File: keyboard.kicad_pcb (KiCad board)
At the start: 2 copper layers, 285 x 94.6 mm, 190 parts, among them IC1 ATMEGA32U4, J1 MINI, P1 CONN_1, P10 CONN_1, P16 CONN_1, P17 CONN_1, P2 CONN_1, P3 CONN_1, P37 CONN_1, P38 CONN_1, P39 CONN_1, P4 CONN_1, P40 CONN_1, P41 CONN_1, P42 CONN_1, P5 CONN_1, P6 CONN_1, P7 CONN_1, P8 CONN_1, P9 CONN_1, X1 ASX3F

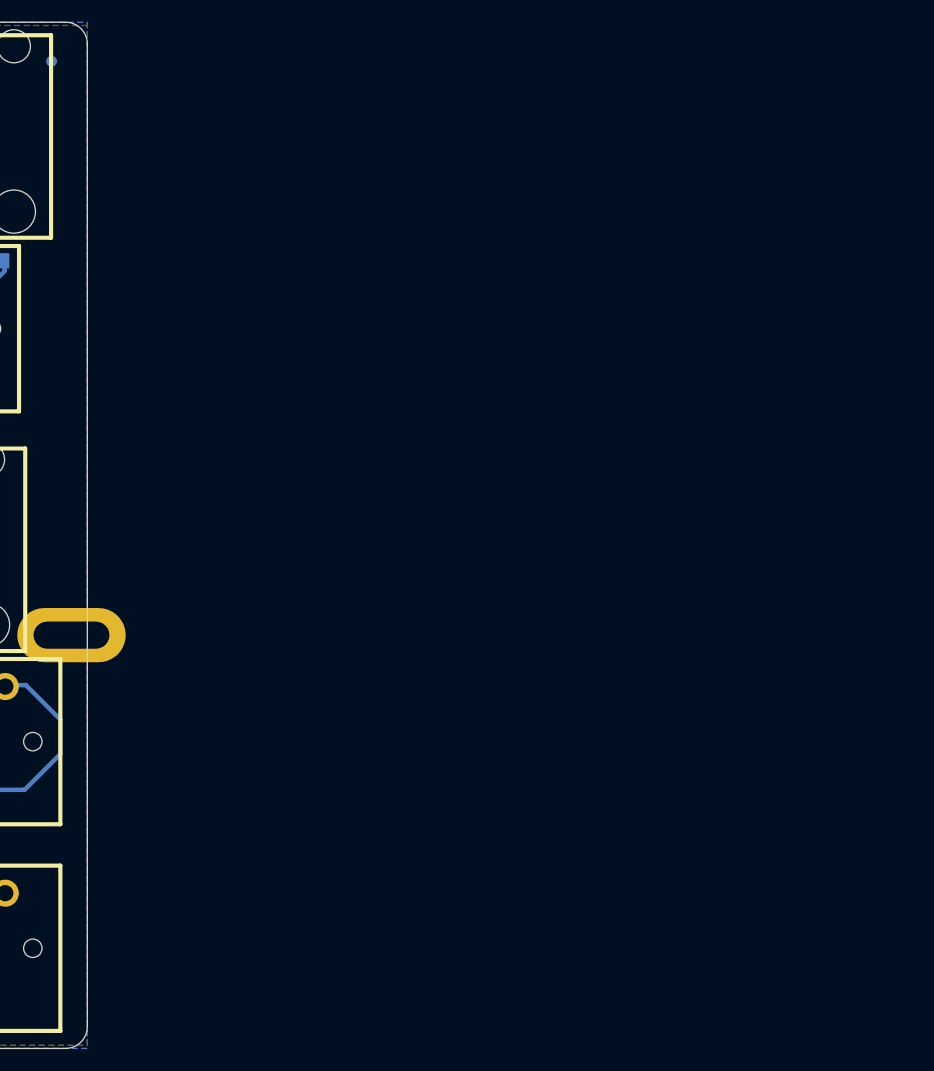
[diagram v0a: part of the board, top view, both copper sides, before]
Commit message: Extend edge cuts to accommodate numpad
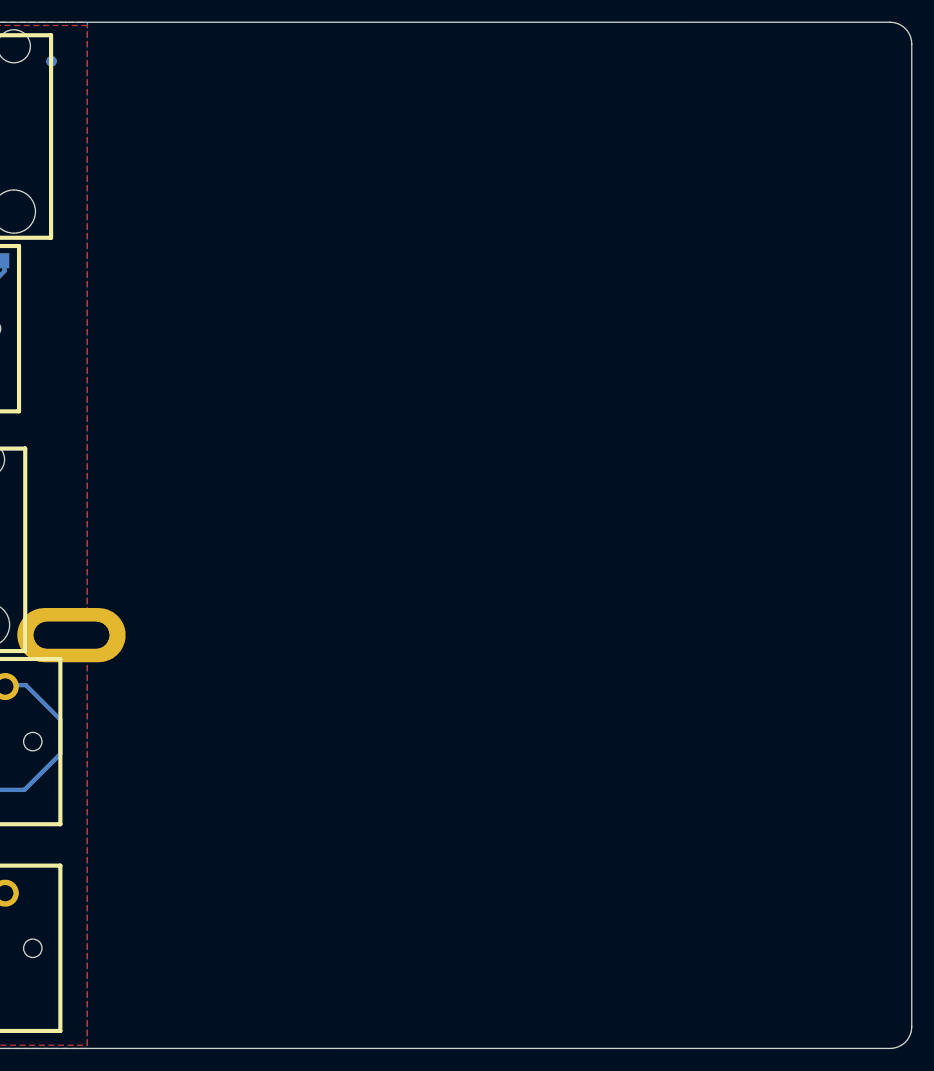
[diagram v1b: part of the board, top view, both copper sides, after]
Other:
- board size 285 x 94.6 mm -> 361 x 94.6 mm
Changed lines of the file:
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@@
   (general
     (thickness 1.6002)
-    (drawings 323)
+    (drawings 325)
     (tracks 2026)
     (zones 0)
@@
   )
   (layers
-    (0 F.Cu signal)
+    (0 F.Cu signal hide)
     (31 B.Cu signal hide)
     (32 B.Adhes user hide)
@@
     (40 Dwgs.User user)
     (41 Cmts.User user hide)
-    (42 Eco1.User user)
+    (42 Eco1.User user hide)
     (43 Eco2.User user hide)
-    (44 Edge.Cuts user hide)
+    (44 Edge.Cuts user)
     (48 B.Fab user hide)
     (49 F.Fab user hide)
@@
     )
   )
+  (gr_line (start 345.29 64.62) (end 421.29 64.6212) (layer Edge.Cuts) (width 0.0991))
+  (gr_line (start 345.29 159.22) (end 421.29 159.2212) (layer Edge.Cuts) (width 0.0991))
+  (gr_arc (start 421.29 66.6212) (end 421.29 64.6212) (angle 90) (layer Edge.Cuts) (width 0.0991))
+  (gr_arc (start 421.29 157.2212) (end 423.29 157.2212) (angle 90) (layer Edge.Cuts) (width 0.0991))
+  (gr_line (start 423.29 66.62) (end 423.29 157.2224) (angle 90) (layer Edge.Cuts) (width 0.0991))
   (gr_line (start 346.75064 140.12672) (end 403.75064 140.13434) (layer Dwgs.User) (width 0.381))
   (gr_line (start 346.75064 83.12658) (end 422.75064 83.1342) (layer Dwgs.User) (width 0.381))
@@
   (gr_arc (start 64.29 66.62) (end 62.29 66.62) (angle 90) (layer Edge.Cuts) (width 0.0991))
   (gr_arc (start 64.29 157.22) (end 64.29 159.22) (angle 90) (layer Edge.Cuts) (width 0.0991))
-  (gr_arc (start 345.29 157.22) (end 347.29 157.22) (angle 90) (layer Edge.Cuts) (width 0.0991))
-  (gr_arc (start 345.29 66.62) (end 345.29 64.62) (angle 90) (layer Edge.Cuts) (width 0.0991))
   (gr_line (start 62.29 157.2212) (end 62.29 66.6188) (angle 90) (layer Edge.Cuts) (width 0.0991))
   (gr_line (start 345.29 159.22) (end 64.29 159.22) (angle 90) (layer Edge.Cuts) (width 0.0991))
-  (gr_line (start 347.29 66.6188) (end 347.29 157.2212) (angle 90) (layer Edge.Cuts) (width 0.0991))
   (gr_line (start 64.29 64.62) (end 345.29 64.62) (angle 90) (layer Edge.Cuts) (width 0.0991))
   (gr_line (start 330.12888 214.94242) (end 330.12888 130.62966) (angle 90) (layer Eco2.User) (width 0.381))

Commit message: Remove GPIOs
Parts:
- removed P10, P38, P39, P40, P41, P7, P8, P9: CONN_1, pad
- removed R10, R11, R12, R6, R7, R8, R9: R, res:resistor
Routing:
- net /GPIO1: track 398.3 -> 0.00 mm, vias 4 -> 0
- net /GPIO3: track 385.2 -> 0.00 mm, vias 7 -> 0
- net /GPIO2: track 372.2 -> 0.00 mm, vias 6 -> 0
- net /GPIO0: track 291.9 -> 0.00 mm, vias 5 -> 0
- net /row5: track 327.2 -> 313.9 mm

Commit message: Start remapping of rows and cols in MCU
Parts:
- removed MXWIRE (x4): VAL**, MX1A-wire
- removed P1, P16, P17, P2, P3, P37, P4, P42, P5, P6: CONN_1, pad
- moved R3 12.6 mm to (154.0, 155.6)
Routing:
- net GND: track 686.3 -> 75.8 mm, vias 41 -> 0
- net VCC: track 384.0 -> 217.1 mm, vias 6 -> 0
- net /col13: track 239.2 -> 85.7 mm, vias 2 -> 0
- net /col12: track 225.0 -> 91.9 mm, vias 2 -> 0
- net /row5: track 313.9 -> 201.1 mm, vias 2 -> 0
- net /col11: track 203.0 -> 90.5 mm, vias 2 -> 0
- net /col1: track 166.1 -> 68.7 mm, vias 2 -> 0
- net /col10: track 185.8 -> 92.1 mm, vias 2 -> 0
- net /MOSI: track 85.2 -> 0.00 mm, vias 1 -> 0
- net /col6: track 156.9 -> 94.8 mm
- net /col9: track 129.9 -> 67.9 mm, vias 2 -> 0
- net /col2: track 143.4 -> 81.5 mm, vias 4 -> 2
- net /col4: track 106.4 -> 56.4 mm, vias 2 -> 0
- net /MISO: track 324.3 -> 278.1 mm, vias 5 -> 4
- net /~RES~: track 179.2 -> 133.7 mm
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
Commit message: Connected all rows in PCB
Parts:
- removed FID (x2): FIDUCIAL, hole:FIDUCIAL
- moved C3 7.93 mm to (161.7, 139.8), turned to 90 degrees
- moved R3 4.24 mm to (150.7, 152.8), turned to 90 degrees
- moved C6 3.41 mm to (168.5, 155.7), turned to 0 degrees
- moved C4 0.68 mm to (152.7, 152.7), turned to 90 degrees
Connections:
- net /GPIO0 renamed Net-(IC1-Pad36)
- net /GPIO1 renamed Net-(IC1-Pad37)
- net /GPIO2 renamed Net-(IC1-Pad38)
- net /GPIO3 renamed Net-(IC1-Pad39)
- net /~RES~ renamed Net-(IC1-Pad13)
- D36 pad 1: /SCK -> /col8
- D37 pad 1: /SCK -> /col8
- D38 pad 1: /SCK -> /col8
- D39 pad 1: /SCK -> /col8
- D66 pad 1: /MISO -> /col14
- D67 pad 1: /MISO -> /col14
- D68 pad 1: /MISO -> /col14
- D69 pad 1: /MISO -> /col14
- D70 pad 1: /MISO -> /col14
- IC1 pad 1: /col3 -> Net-(IC1-Pad1)
- IC1 pad 10: /MOSI -> /row3
- IC1 pad 11: /MISO -> /row4
- IC1 pad 12: /col9 -> Net-(IC1-Pad12)
- IC1 pad 18: /row1 -> Net-(IC1-Pad18)
- IC1 pad 19: /row2 -> Net-(IC1-Pad19)
- IC1 pad 20: /row3 -> Net-(IC1-Pad20)
- IC1 pad 21: /row4 -> Net-(IC1-Pad21)
- IC1 pad 25: /col7 -> Net-(IC1-Pad25)
- IC1 pad 26: /col13 -> Net-(IC1-Pad26)
- IC1 pad 27: /col12 -> Net-(IC1-Pad27)
- IC1 pad 28: /col11 -> Net-(IC1-Pad28)
- IC1 pad 29: /col10 -> Net-(IC1-Pad29)
- IC1 pad 30: /col6 -> Net-(IC1-Pad30)
- IC1 pad 31: /col5 -> Net-(IC1-Pad31)
- IC1 pad 32: /col4 -> Net-(IC1-Pad32)
- IC1 pad 40: /col2 -> Net-(IC1-Pad40)
- IC1 pad 41: /col1 -> Net-(IC1-Pad41)
- IC1 pad 8: Net-(IC1-Pad8) -> /row1
- IC1 pad 9: /SCK -> /row2
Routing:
- net /MISO: track 278.1 -> 0.00 mm, vias 4 -> 0
- net /SCK: track 117.9 -> 0.00 mm, vias 2 -> 0
- net /col14: track 0.00 -> 97.1 mm
- net /row5: track 201.1 -> 293.8 mm
- net /col8: track 0.00 -> 68.5 mm
- net GND: track 75.8 -> 11.3 mm, vias 0 -> 4
- net /row3: track 330.5 -> 317.3 mm, vias 3 -> 1
- net /row2: track 373.0 -> 360.6 mm, vias 3 -> 1
- net Net-(C3-Pad1): track 11.6 -> 2.60 mm
- net /row1: track 401.5 -> 393.5 mm, vias 2 -> 0
- net /row4: track 334.5 -> 326.6 mm, vias 3 -> 1
- net VCC: track 217.1 -> 210.0 mm
- net Net-(IC1-Pad33): track 2.74 -> 7.25 mm

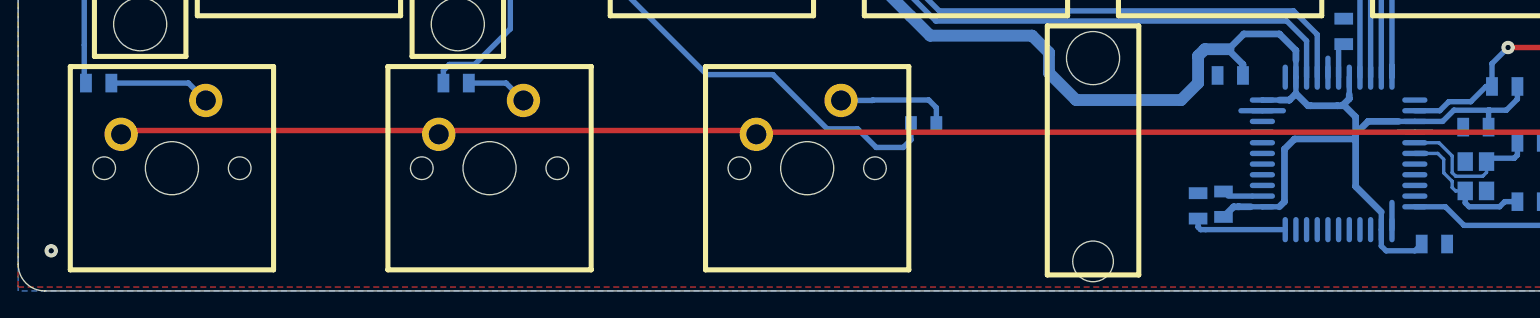
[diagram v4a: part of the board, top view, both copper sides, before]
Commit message: Connect cols 1 to 3
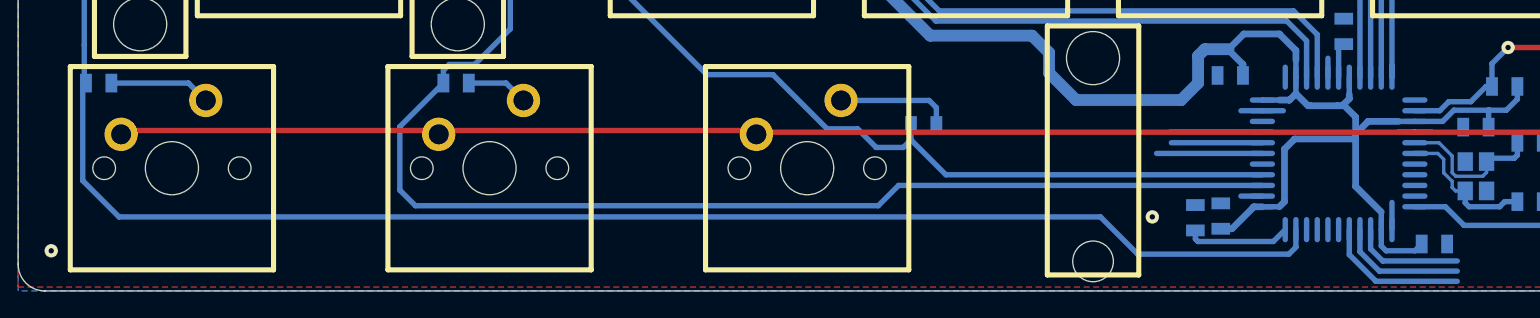
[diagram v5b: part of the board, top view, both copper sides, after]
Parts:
- moved C4 0.91 mm to (152.5, 153.6)
- moved R3 0.91 mm to (150.5, 153.7)
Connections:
- IC1 pad 32: Net-(IC1-Pad32) -> /col1
- IC1 pad 36: Net-(IC1-Pad36) -> /col2
- IC1 pad 37: Net-(IC1-Pad37) -> /col3
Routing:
- net /col1: track 68.7 -> 170.8 mm
- net /col2: track 81.5 -> 156.7 mm
- net /col3: track 105.4 -> 132.8 mm
- net Net-(IC1-Pad27): track 0.00 -> 10.8 mm
- net Net-(IC1-Pad26): track 0.00 -> 9.55 mm
- net Net-(IC1-Pad25): track 0.00 -> 8.31 mm
- net Net-(IC1-Pad39): track 0.00 -> 7.93 mm
- net Net-(IC1-Pad41): track 0.00 -> 6.97 mm
- net Net-(IC1-Pad40): track 0.00 -> 6.82 mm
- net VCC: track 210.0 -> 211.4 mm
- net Net-(IC1-Pad33): track 7.25 -> 7.82 mm
- net GND: track 11.3 -> 11.1 mm, vias 4 -> 5

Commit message: Connect col4
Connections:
- IC1 pad 38: Net-(IC1-Pad38) -> /col4
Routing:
- net /col4: track 56.4 -> 105.4 mm, vias 0 -> 2

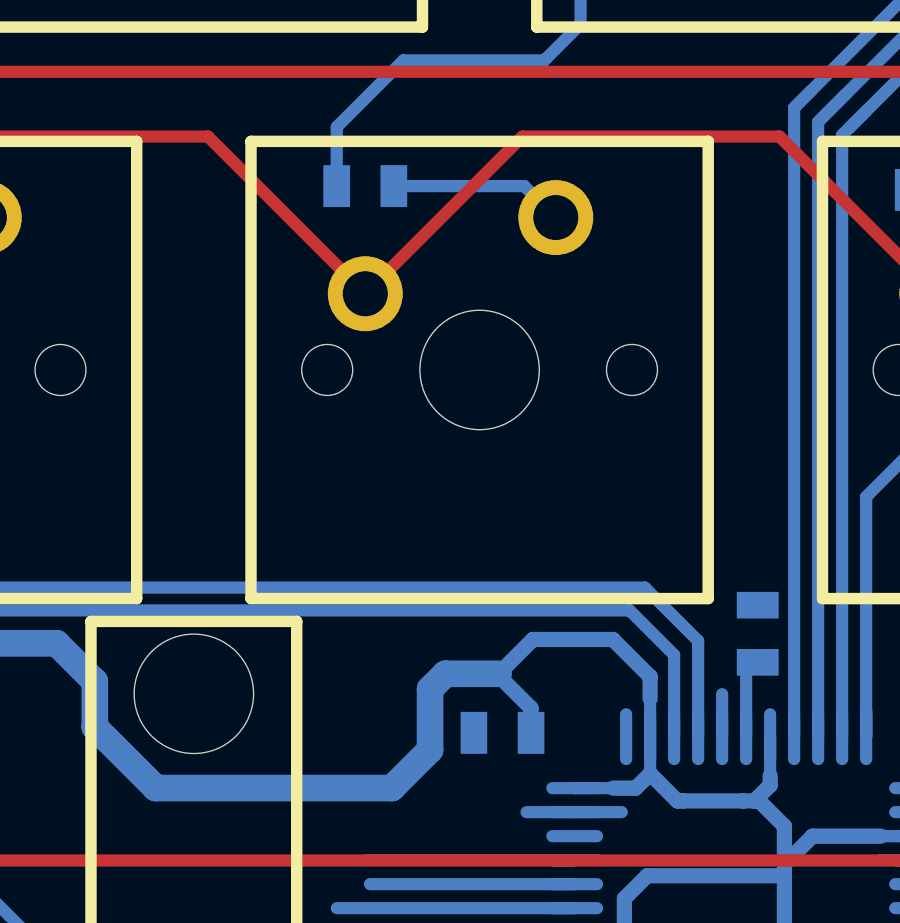
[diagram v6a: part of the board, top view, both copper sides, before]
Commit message: Connect col5
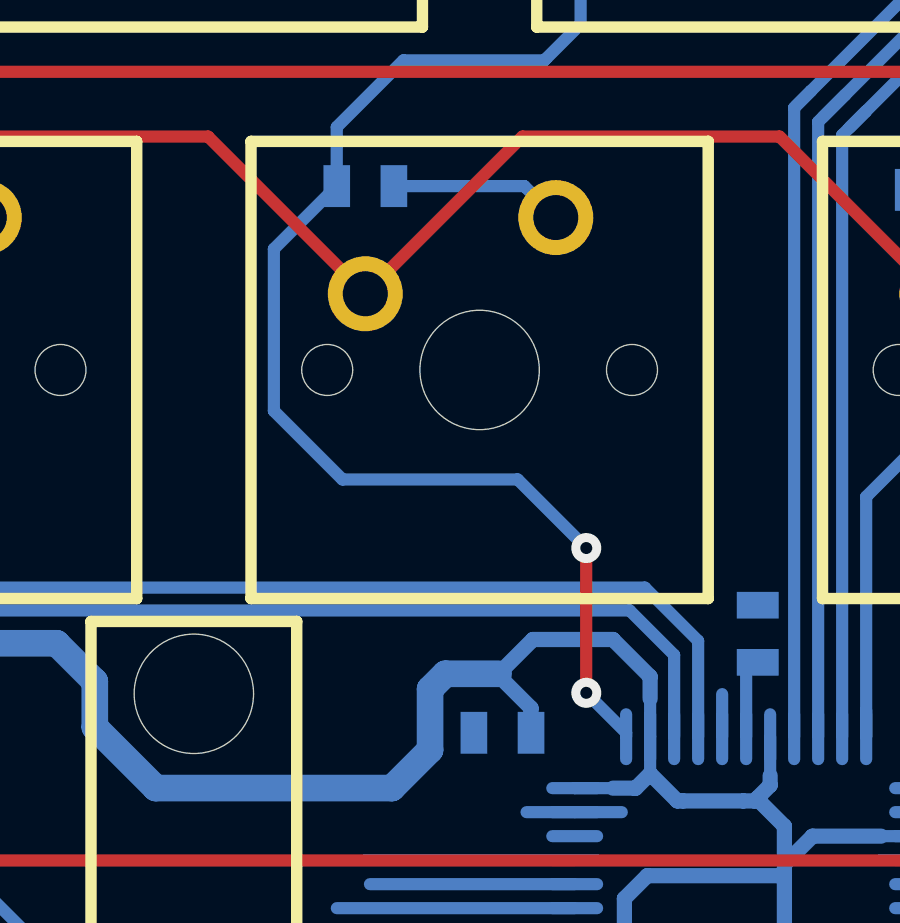
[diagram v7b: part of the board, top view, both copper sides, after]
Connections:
- IC1 pad 1: Net-(IC1-Pad1) -> /col5
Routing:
- net /col5: track 60.0 -> 87.5 mm, vias 0 -> 2
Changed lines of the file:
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@@
     (thickness 1.6002)
     (drawings 325)
-    (tracks 1204)
+    (tracks 1215)
     (zones 0)
     (modules 159)
-    (nets 114)
+    (nets 113)
   )
   (page A2)
@@
   (net 111 "Net-(IC1-Pad30)")
   (net 112 "Net-(IC1-Pad31)")
-  (net 113 "Net-(IC1-Pad1)")
   (net_class Default "This is the default net class."
     (clearance 0.2032)
@@
     (add_net "Net-(D70-Pad2)")
     (add_net "Net-(D71-Pad2)")
-    (add_net "Net-(IC1-Pad1)")
     (add_net "Net-(IC1-Pad12)")
     (add_net "Net-(IC1-Pad13)")
@@
       (net 86 "Net-(IC1-Pad33)"))
     (pad 1 smd oval (at -5.715 4.0005 270) (size 1.89992 0.4064) (layers B.Cu B.Paste B.Mask)
-      (net 113 "Net-(IC1-Pad1)"))
+      (net 28 /col5))
     (model ${KIPRJMOD}/lib/tqfp.pretty/ipc_tqfp.wrl
       (at (xyz 0 0 0))
@@
   (segment (start 155.56992 152.11044) (end 153.95956 152.11044) (width 0.4064) (layer B.Cu) (net 1))
   (via (at 147.32 153.67) (size 1) (drill 0.4) (layers F.Cu B.Cu) (net 1))
+  (via (at 155.956 141.732) (size 1) (drill 0.4) (layers F.Cu B.Cu) (net 28))
   (segment (start 155.56992 144.90954) (end 155.57246 144.907) (width 0.4064) (layer B.Cu) (net 2))
   (segment (start 83.48726 84.75726) (end 87.503 84.75726) (width 0.889) (layer B.Cu) (net 2))
@@
   (segment (start 149.479 88.9) (end 149.479 95.25) (width 0.4064) (layer B.Cu) (net 28))
   (segment (start 150.8125 97.409) (end 150.8125 96.5835) (width 0.4064) (layer B.Cu) (net 28))
+  (segment (start 157.28442 143.06042) (end 155.956 141.732) (width 0.4064) (layer B.Cu) (net 28))
+  (segment (start 157.28442 143.19504) (end 157.28442 143.06042) (width 0.4064) (layer B.Cu) (net 28))
+  (segment (start 155.956 141.732) (end 155.956 136.906) (width 0.4064) (layer F.Cu) (net 28))
+  (segment (start 155.956 136.906) (end 155.956 136.906) (width 0.4064) (layer F.Cu) (net 28))
+  (via (at 155.956 136.906) (size 1) (drill 0.4) (layers F.Cu B.Cu) (net 28))
+  (segment (start 145.542 126.9365) (end 147.6375 124.841) (width 0.4064) (layer B.Cu) (net 28))
+  (segment (start 145.542 132.334) (end 145.542 126.9365) (width 0.4064) (layer B.Cu) (net 28))
+  (segment (start 147.828 134.62) (end 145.542 132.334) (width 0.4064) (layer B.Cu) (net 28))
+  (segment (start 153.67 134.62) (end 147.828 134.62) (width 0.4064) (layer B.Cu) (net 28))
+  (segment (start 155.956 136.906) (end 153.67 134.62) (width 0.4064) (layer B.Cu) (net 28))
   (segment (start 150.79726 69.52234) (end 150.1775 68.74002) (width 0.4064) (layer B.Cu) (net 29))
   (segment (start 144.018 78.359) (end 145.415 76.962) (width 0.4064) (layer B.Cu) (net 29))
